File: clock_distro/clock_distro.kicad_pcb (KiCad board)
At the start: 4 copper layers, 41.9 x 111.8 mm, 37 parts, among them J1 SMA, J10 SMA, J2 SMA, J3 SMA, J4 SMA, J5 SMA, J6 SMA, J7 SMA, J8 SMA, J9 SMA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

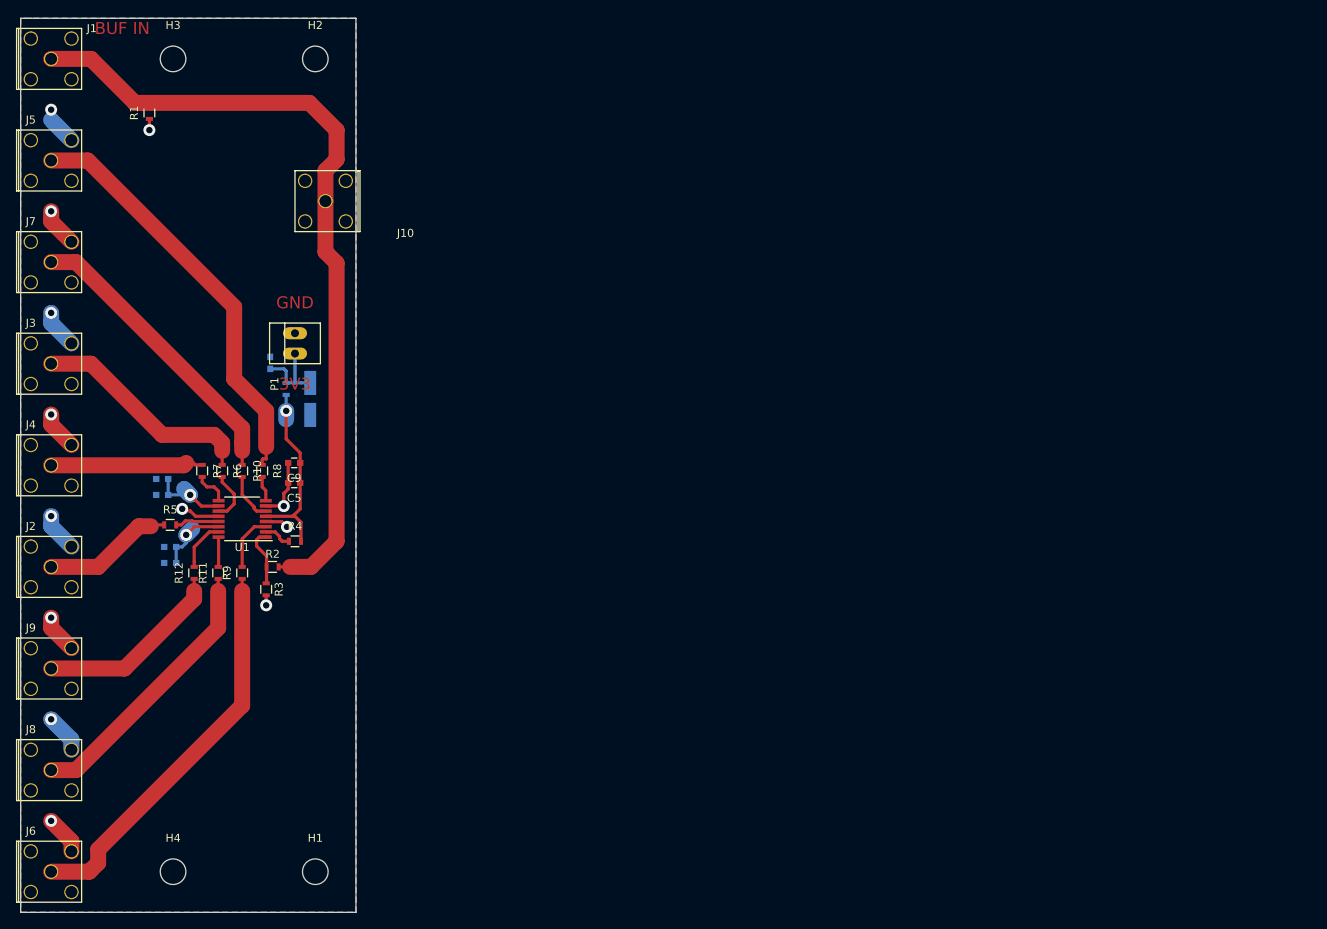
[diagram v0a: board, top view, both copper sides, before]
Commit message: added bc637 pcie dsub15 clock/pps breakout
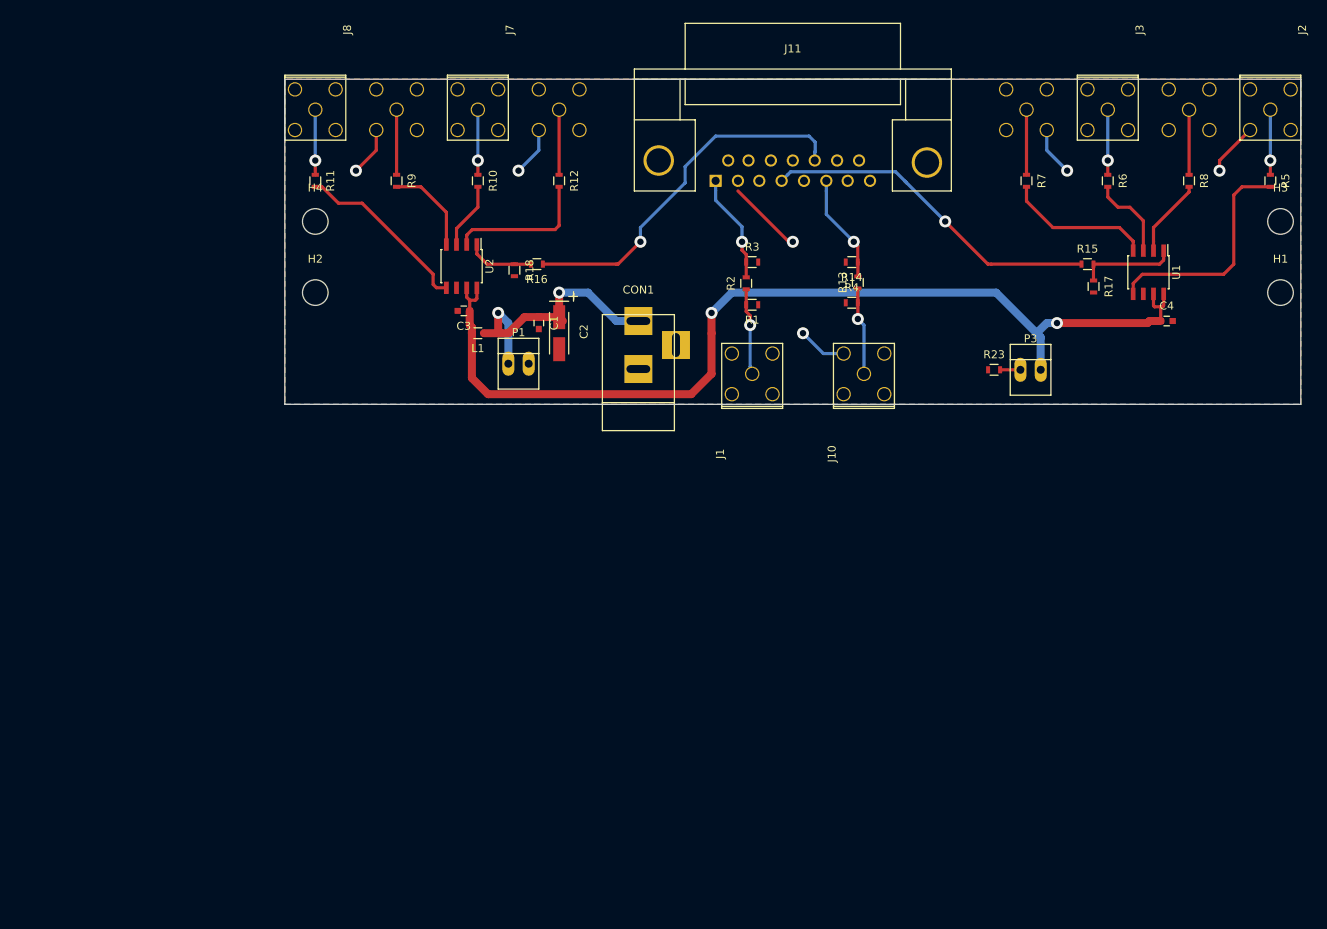
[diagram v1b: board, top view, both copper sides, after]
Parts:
- removed C10, C9: 1 uF, Capacitors_SMD:C_0603
- removed C5, C7, C8: 100 nF, Capacitors_SMD:C_0603
- added C3: 100 nF, Capacitors_SMD:C_0603, F.Cu at (122.7, 95.0)
- added CON1: BARREL_JACK, Connect:BARREL_JACK, F.Cu at (144.5, 102.5)
- added J11: DB15, Connect:DB15FC, F.Cu at (163.8, 77.5)
- added P3: CONN_01X02, Connect:PINHEAD1-2, F.Cu at (193.5, 102.4)
- added R13: 18, Resistors_SMD:R_0603, F.Cu at (172.0, 91.4)
- added R14: 33, Resistors_SMD:R_0603, F.Cu at (171.2, 88.9)
- added R15: 18, Resistors_SMD:R_0603, F.Cu at (200.7, 89.2)
- added R16: 18, Resistors_SMD:R_0603, F.Cu at (131.8, 89.2)
- added R17: 33, Resistors_SMD:R_0603, F.Cu at (201.4, 91.9)
- added R18: 33, Resistors_SMD:R_0603, F.Cu at (129.0, 89.9)
- added R23: 1k, Resistors_SMD:R_0603, F.Cu at (189.0, 102.4)
- added U2: NB3N551, Housings_SOIC:SOIC-8_3.9x4.9mm_Pitch1.27mm, F.Cu at (122.4, 89.4)
- C1, C2, L1: moved to F.Cu
- C4: value 1 uF -> 100 nF; moved to F.Cu
- J4, J5, J6, J9: moved to B.Cu
- R10, R11, R12, R5, R6, R7, R8, R9: value 10 -> 30
- R4: value 10k -> DNP
- U1: value CDCLVC1108 -> NB3N551; footprint Housings_SSOP:TSSOP-16_4.4x5mm_Pitch0.65mm -> Housings_SOIC:SOIC-8_3.9x4.9mm_Pitch1.27mm
- moved J2 162.8 mm to (223.5, 69.8), turned to 270 degrees
- moved R5 144.1 mm to (223.5, 78.7), turned to 270 degrees
- moved J5 142.4 mm to (213.4, 69.8), turned to 270 degrees
- moved H1 140.7 mm to (224.8, 92.7)
- moved H3 139.9 mm to (224.8, 83.8)
- moved J3 135.8 mm to (203.2, 69.8), turned to 270 degrees
- moved J4 129.8 mm to (193.0, 69.8), turned to 270 degrees
- moved C4 127.1 mm to (210.6, 96.3), turned to 0 degrees
- moved R8 121.4 mm to (213.4, 78.7)
- moved U1 117.4 mm to (208.3, 90.2), turned to 270 degrees
- moved R6 116.5 mm to (203.2, 78.7)
- moved R7 109.2 mm to (193.0, 78.7)
- moved J6 104.6 mm to (114.3, 69.8), turned to 270 degrees
- moved J1 96.1 mm to (158.8, 102.9), turned to 90 degrees
- moved J9 94.4 mm to (134.6, 69.8), turned to 270 degrees
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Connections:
- C4 pad 1: +3V3 -> +5V
- J10 pad 1: Net-(J1-Pad1) -> Net-(J10-Pad1)
- L1 pad 2: +3V3 -> +5V
- R10 pad 2: /Y4 -> /PPS2
- R11 pad 2: /Y1 -> /PPS4
- R12 pad 2: /Y3 -> /PPS1
- R2 pad 2: Net-(R2-Pad2) -> /EXT_10MHZ_IN
- R3 pad 1: Net-(R2-Pad2) -> /EXT_10MHZ_IN
- R4 pad 1: Net-(R4-Pad1) -> GND
- R4 pad 2: +3V3 -> Net-(J10-Pad1)
- R5 pad 2: /Y2 -> /10M4
- R6 pad 2: /Y5 -> /10M2
- R7 pad 2: /Y7 -> /10M3
- R8 pad 2: /Y6 -> /10M1
- R9 pad 2: /Y0 -> /PPS3
- U1 pad 1: Net-(R2-Pad2) -> Net-(R15-Pad2)
- U1 pad 2: Net-(R4-Pad1) -> /10M1
- U1 pad 3: /Y0 -> /10M2
- U1 pad 4: GND -> /10M3
- U1 pad 5: +3V3 -> /10M4
- U1 pad 6: /Y4 -> GND
- U1 pad 7: GND -> +5V
- U1 pad 8: /Y6 -> +5V
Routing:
- net +5V: track 0.00 -> 124.2 mm, vias 0 -> 2
- net Net-(J1-Pad1): track 101.9 -> 10.2 mm, vias 0 -> 1
- net +3V3: track 69.1 -> 0.00 mm, vias 3 -> 0
- net /10MPPS_OUT: track 0.00 -> 45.5 mm, vias 0 -> 1
- net Net-(J5-Pad1): track 52.3 -> 8.14 mm
- net /1PPS_OUT: track 0.00 -> 43.1 mm, vias 0 -> 1
- net Net-(J6-Pad1): track 49.3 -> 8.14 mm
- net Net-(J7-Pad1): track 37.1 -> 8.14 mm, vias 0 -> 1
- net /10M4: track 0.00 -> 28.5 mm
- net Net-(J8-Pad1): track 34.4 -> 8.14 mm, vias 0 -> 1
- net GND: track 57.3 -> 31.2 mm, vias 13 -> 5
- net Net-(C1-Pad1): track 10.3 -> 34.8 mm, vias 0 -> 2
- net /PPS4: track 0.00 -> 22.4 mm
- net Net-(J3-Pad1): track 28.2 -> 8.14 mm, vias 0 -> 1
- net /10M3: track 0.00 -> 18.4 mm
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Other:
- board size 41.9 x 111.8 mm -> 127 x 40.6 mm
- board text removed: "3V3"
- board text removed: "BUF IN"
- board text removed: "GND"

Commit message: length tuned clock/pps traces, switch dsub15 connector to male
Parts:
- J11: footprint Connect:DB15FC -> Connect:DB15MC
- moved H1 10.2 mm to (223.5, 102.9)
- moved H2 10.2 mm to (104.1, 102.9)
- moved H3 1.27 mm to (223.5, 83.8)
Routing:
- net /10M1: track 9.82 -> 22.4 mm
- net /EXT_EVENT_IN: track 13.6 -> 25.4 mm
- net /10M2: track 10.7 -> 22.3 mm
- net /EXT_10MHZ_IN: track 13.6 -> 24.5 mm
- net /PPS3: track 11.6 -> 22.4 mm
- net /PPS2: track 8.32 -> 17.7 mm
- net (no net): track 9.49 -> 0.51 mm
- net /10MPPS_OUT: track 45.5 -> 39.6 mm
- net /10M4: track 28.5 -> 23.5 mm
- net GND: track 31.2 -> 35.8 mm, vias 5 -> 7
- net /PPS1: track 18.1 -> 21.6 mm
- net /10M3: track 18.4 -> 21.6 mm
- net /1PPS_OUT: track 43.1 -> 40.4 mm

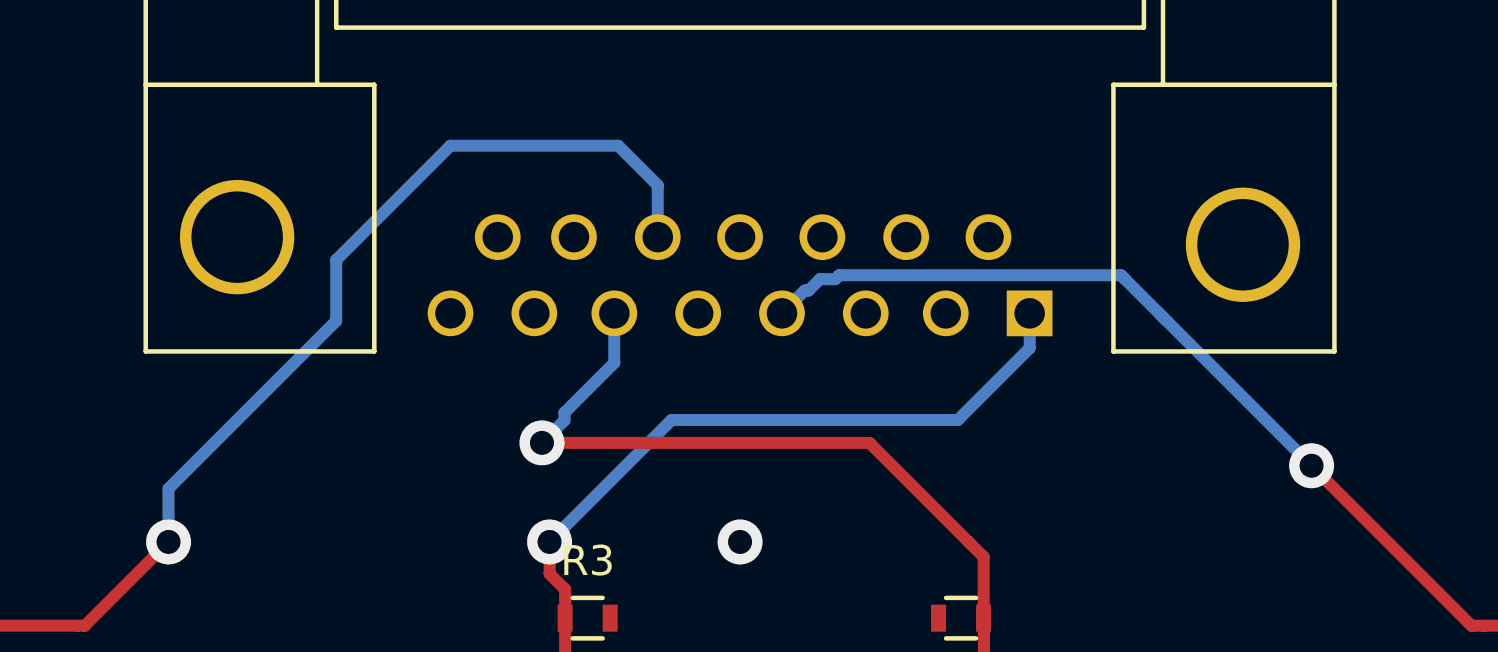
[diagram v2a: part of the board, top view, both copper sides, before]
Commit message: fixed dsub 15 connector footprint - moved mounting holes
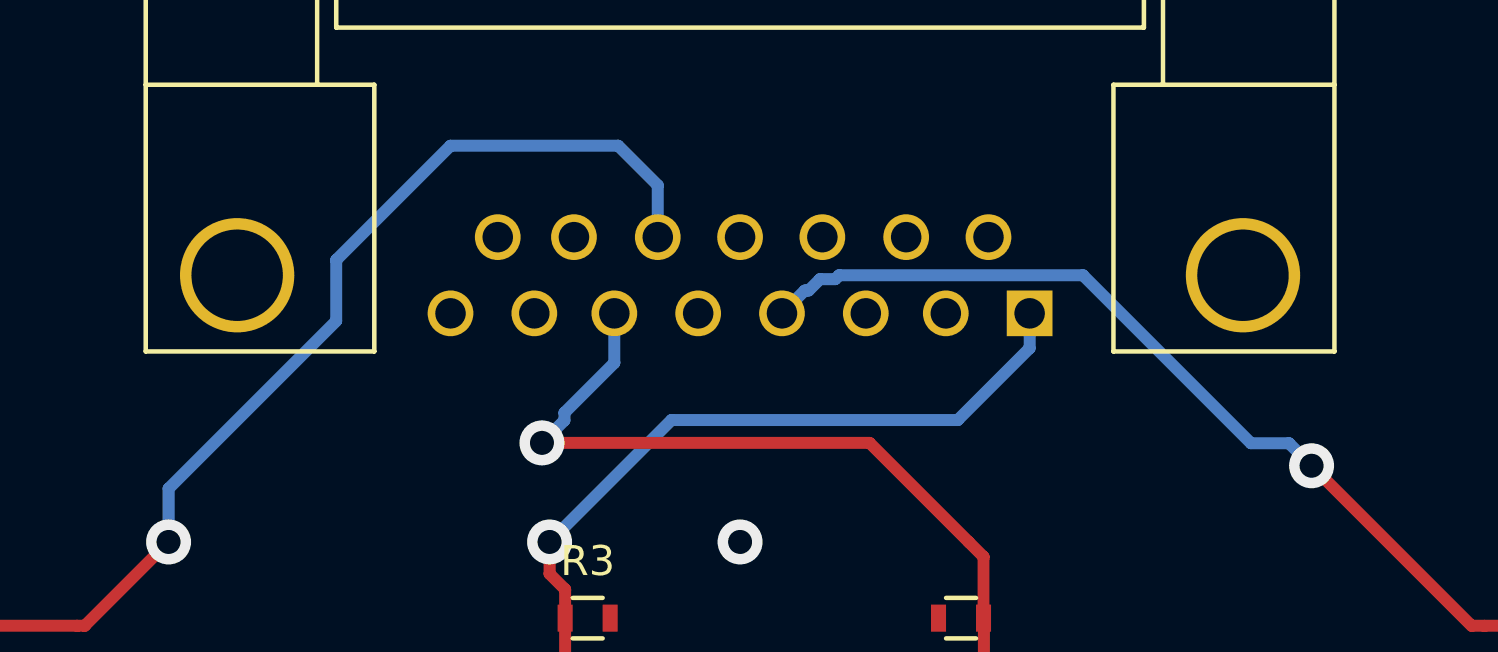
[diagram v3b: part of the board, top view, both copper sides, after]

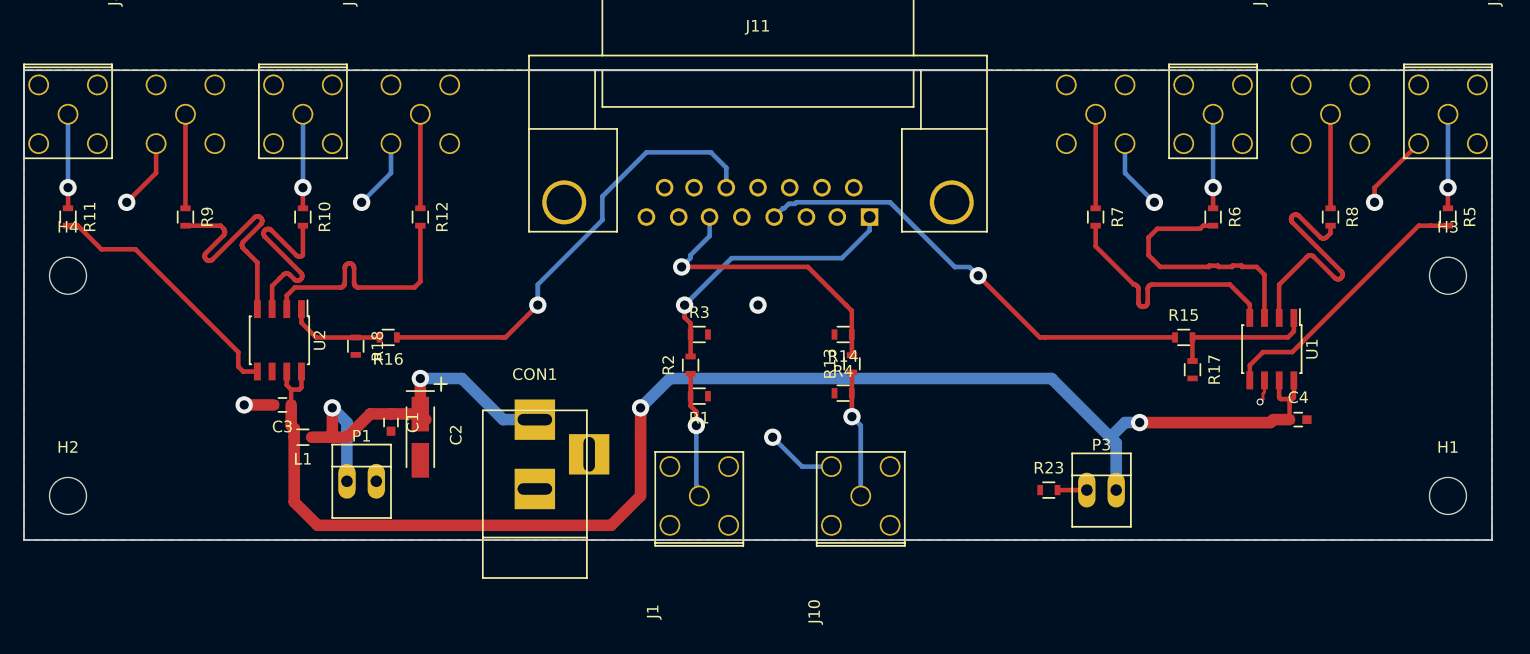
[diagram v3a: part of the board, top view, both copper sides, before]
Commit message: moved headers on isolation boards to match actual measurements on lfrx and lftx usrp daughterboards, ready to order
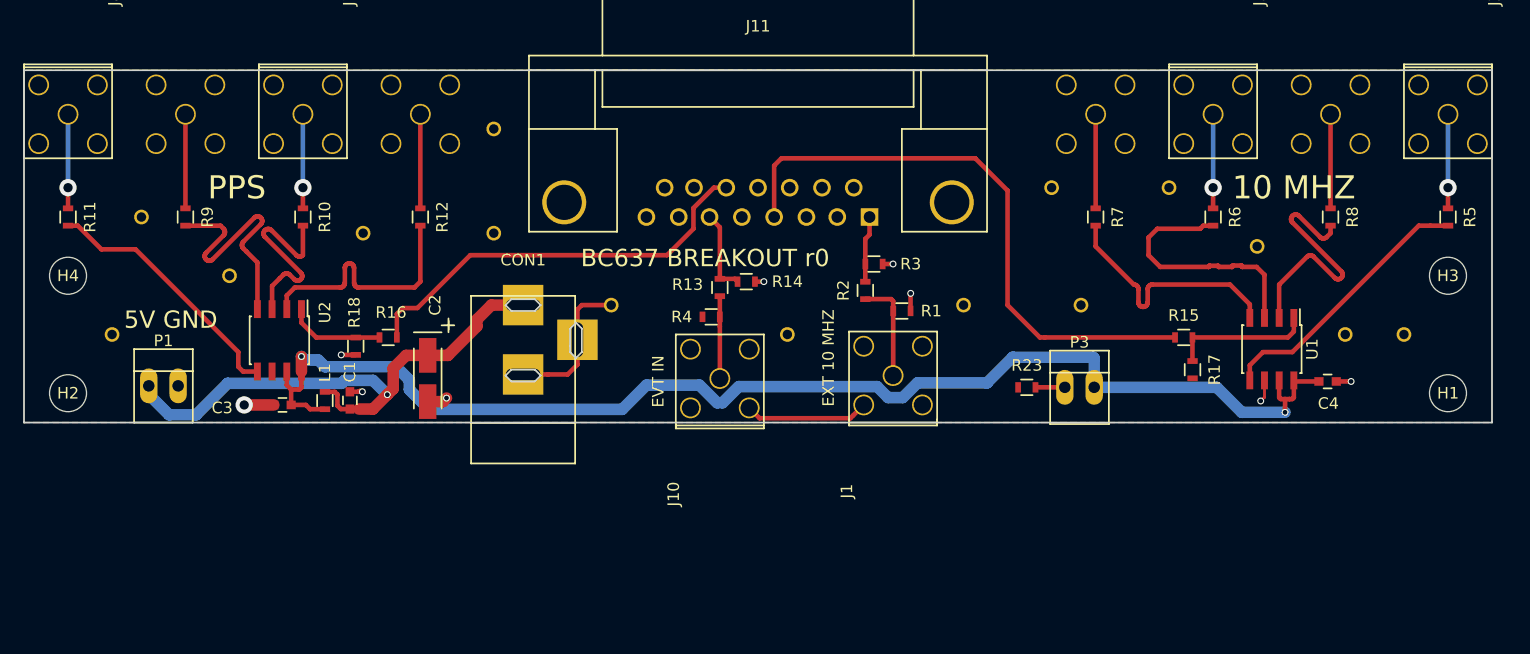
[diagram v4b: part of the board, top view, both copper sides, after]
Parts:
- added REF**: DRILL_32p25mil, vna_footprints:DRILL_32p25mil, F.Cu at (118.1, 83.8)
- added REF**: DRILL_32p25mil, vna_footprints:DRILL_32p25mil, F.Cu at (189.2, 76.2)
- added REF**: DRILL_32p25mil, vna_footprints:DRILL_32p25mil, F.Cu at (191.8, 86.4)
- added REF**: DRILL_32p25mil, vna_footprints:DRILL_32p25mil, F.Cu at (108.0, 88.9)
- added REF**: DRILL_32p25mil, vna_footprints:DRILL_32p25mil, F.Cu at (110.5, 78.7)
- added REF**: DRILL_32p25mil, vna_footprints:DRILL_32p25mil, F.Cu at (141.0, 80.1)
- added REF**: DRILL_32p25mil, vna_footprints:DRILL_32p25mil, F.Cu at (129.7, 80.1)
- added REF**: DRILL_32p25mil, vna_footprints:DRILL_32p25mil, F.Cu at (141.0, 71.1)
- added REF**: DRILL_32p25mil, vna_footprints:DRILL_32p25mil, F.Cu at (151.1, 86.4)
- added REF**: DRILL_32p25mil, vna_footprints:DRILL_32p25mil, F.Cu at (166.4, 88.9)
- added REF**: DRILL_32p25mil, vna_footprints:DRILL_32p25mil, F.Cu at (181.6, 86.4)
- added REF**: DRILL_32p25mil, vna_footprints:DRILL_32p25mil, F.Cu at (207.0, 81.3)
- added REF**: DRILL_32p25mil, vna_footprints:DRILL_32p25mil, F.Cu at (219.7, 88.9)
- added REF**: DRILL_32p25mil, vna_footprints:DRILL_32p25mil, F.Cu at (214.6, 88.9)
- added REF**: DRILL_32p25mil, vna_footprints:DRILL_32p25mil, F.Cu at (199.4, 76.2)
- moved J1 19.7 mm to (175.5, 92.5)
- moved P1 19.0 mm to (112.4, 93.3)
- moved R1 19.0 mm to (176.3, 86.9)
- moved R2 16.4 mm to (173.1, 85.1)
- moved R3 16.3 mm to (173.9, 82.8)
- moved J10 15.9 mm to (160.5, 92.7)
- moved R13 13.2 mm to (160.5, 84.8)
- moved R4 13.2 mm to (159.8, 87.4)
- moved CON1 9.96 mm to (143.5, 92.6)
- moved R14 9.55 mm to (162.8, 84.3), turned to 0 degrees
- moved P3 9.09 mm to (191.6, 93.5)
- moved R23 9.09 mm to (187.1, 93.5)
- moved H1 8.89 mm to (223.5, 94.0)
- moved H2 8.89 mm to (104.1, 94.0)
- moved C2 5.12 mm to (135.3, 92.7)
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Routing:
- net /EXT_10MHZ_IN: track 24.5 -> 5.75 mm, vias 1 -> 0
- net /EXT_EVENT_IN: track 25.4 -> 7.55 mm, vias 1 -> 0
- net Net-(C1-Pad1): track 34.8 -> 47.3 mm, vias 2 -> 1
- net +5V: track 124.2 -> 112.3 mm
- net /1PPS_OUT: track 40.0 -> 51.6 mm, vias 1 -> 0
- net /10MPPS_OUT: track 39.6 -> 36.1 mm, vias 1 -> 0
- net Net-(J10-Pad1): track 10.4 -> 7.12 mm, vias 1 -> 0
- net Net-(J1-Pad1): track 10.2 -> 8.93 mm, vias 1 -> 0
- net GND: track 35.8 -> 36.8 mm, vias 7 -> 9
- net (no net): track 0.51 -> 0.00 mm, vias 1 -> 0
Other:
- board size 127 x 40.6 mm -> 127 x 30.5 mm
- copper layers 4 -> 2
- board text added: "10 MHZ"
- board text added: "5V GND"
- board text added: "BC637 BREAKOUT r0"
- board text added: "EVT IN"
- board text added: "EXT 10 MHZ"
- board text added: "PPS"
